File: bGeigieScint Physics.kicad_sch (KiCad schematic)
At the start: 15 parts, among them P1 Header-Male-2.54_2x2, P2 Header-Male-2.54_2x2, U1 TMP116xxDRV, U2 AT24CS01-STUM, U3 BroadCOM SiPM 4x4

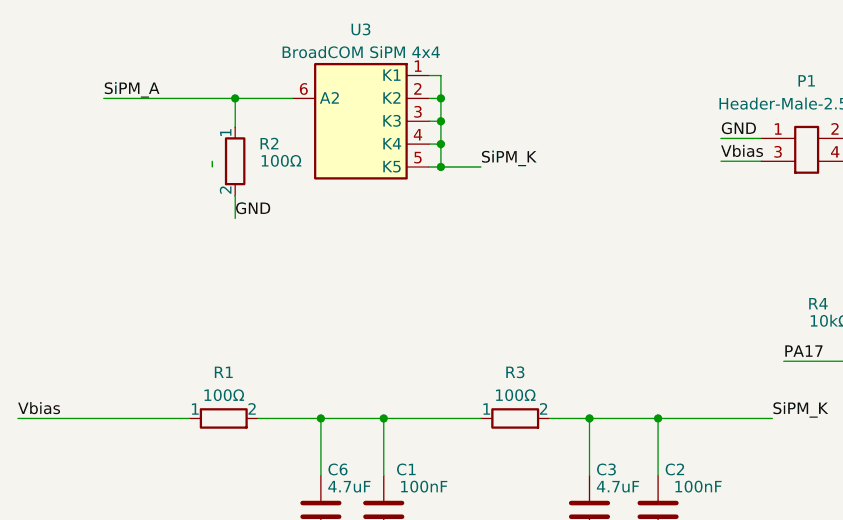
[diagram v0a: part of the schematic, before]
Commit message: Add AFBRS4N44P014M component to KiCad libraries
- Created new module file for AFBRS4N44P014M in Kicad libs with detailed footprint and pad definitions.
- Added corresponding module entry in the bGeigieScint.pretty library.
- Updated fp-lib-table to include new library paths for proper integration.
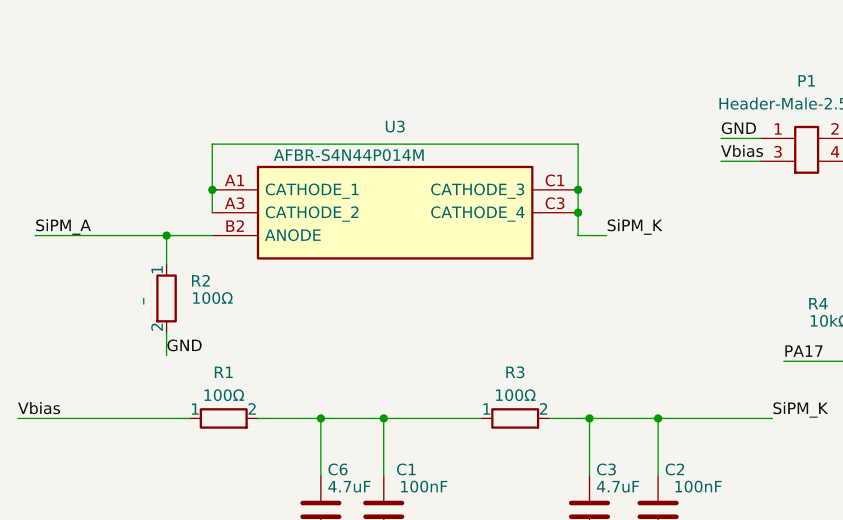
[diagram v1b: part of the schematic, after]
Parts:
- removed U3: BroadCOM SiPM 4x4, symbol SiPM_4x4
- added U3: AFBR-S4N44P014M, AFBRS4N44P014M, symbol AFBR-S4N44P014M:AFBR-S4N44P014M
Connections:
- net SiPM_A: now also U3.B2 (ANODE)
- net SiPM_K: now also U3.A1 (CATHODE_1), U3.A3 (CATHODE_2), U3.C1 (CATHODE_3), U3.C3 (CATHODE_4)
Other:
- moved on the sheet: R2

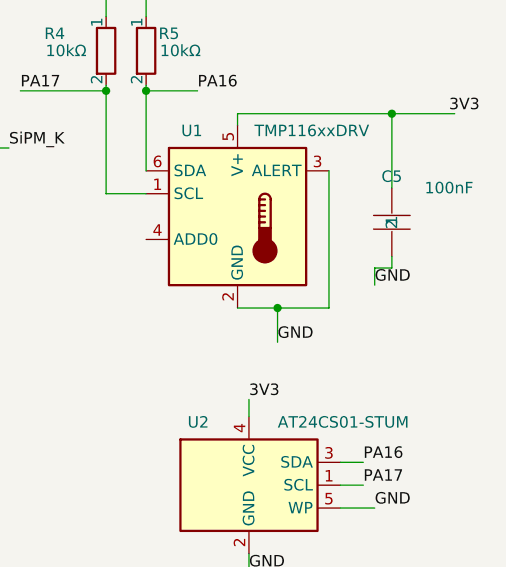
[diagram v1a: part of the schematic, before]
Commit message: refactor: Remove unused schematic symbol definitions, add a 3D model, and update KiCad schematic and PCB files.
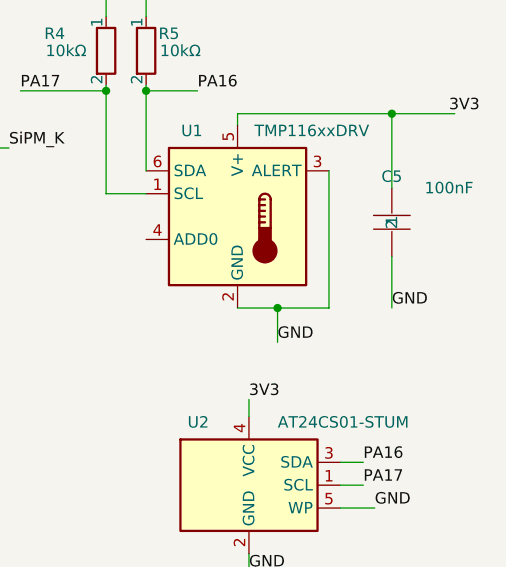
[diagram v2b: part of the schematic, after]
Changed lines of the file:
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@@
-	(wire
-		(pts
-			(xy 167.005 113.665) (xy 167.005 114.935)
-		)
-		(stroke
-			(width 0)
-			(type default)
-		)
-	)
 	(wire
 		(pts
@@
 	(wire
 		(pts
-			(xy 167.005 114.935) (xy 165.1 114.935)
-		)
-		(stroke
-			(width 0)
-			(type default)
-		)
-	)
-	(wire
-		(pts
 			(xy 74.295 101.6) (xy 74.295 107.95)
 		)
@@
 	(wire
 		(pts
-			(xy 165.1 114.935) (xy 165.1 116.84)
+			(xy 167.005 113.665) (xy 167.005 119.38)
 		)
 		(stroke
@@
 	)
 	(label "GND"
-		(at 165.1 116.84 0)
-		(effects
-			(font
+		(at 167.005 119.38 0)
+		(effects
+			(font

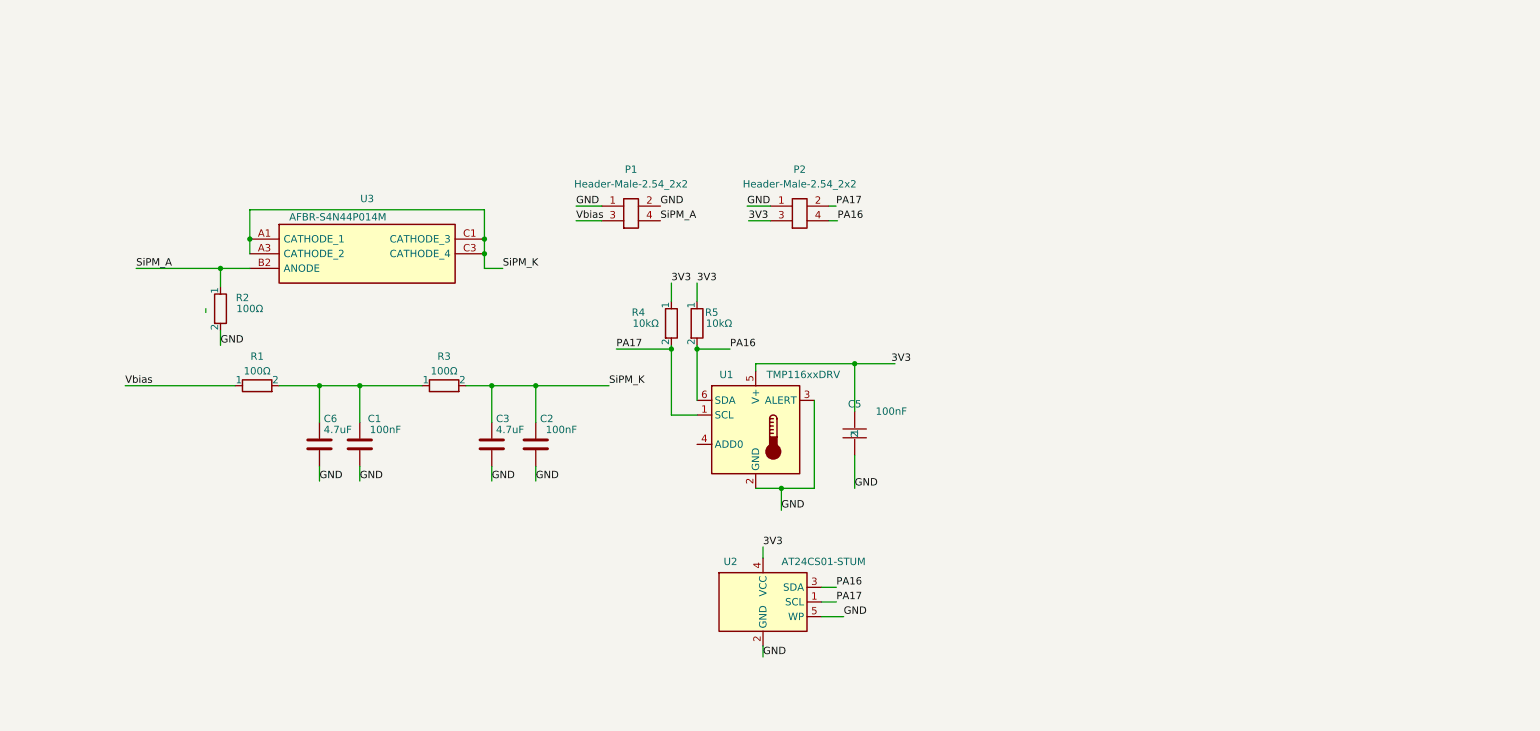
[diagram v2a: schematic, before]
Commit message: feat: Add new KiCad component libraries and update schematic/PCB.
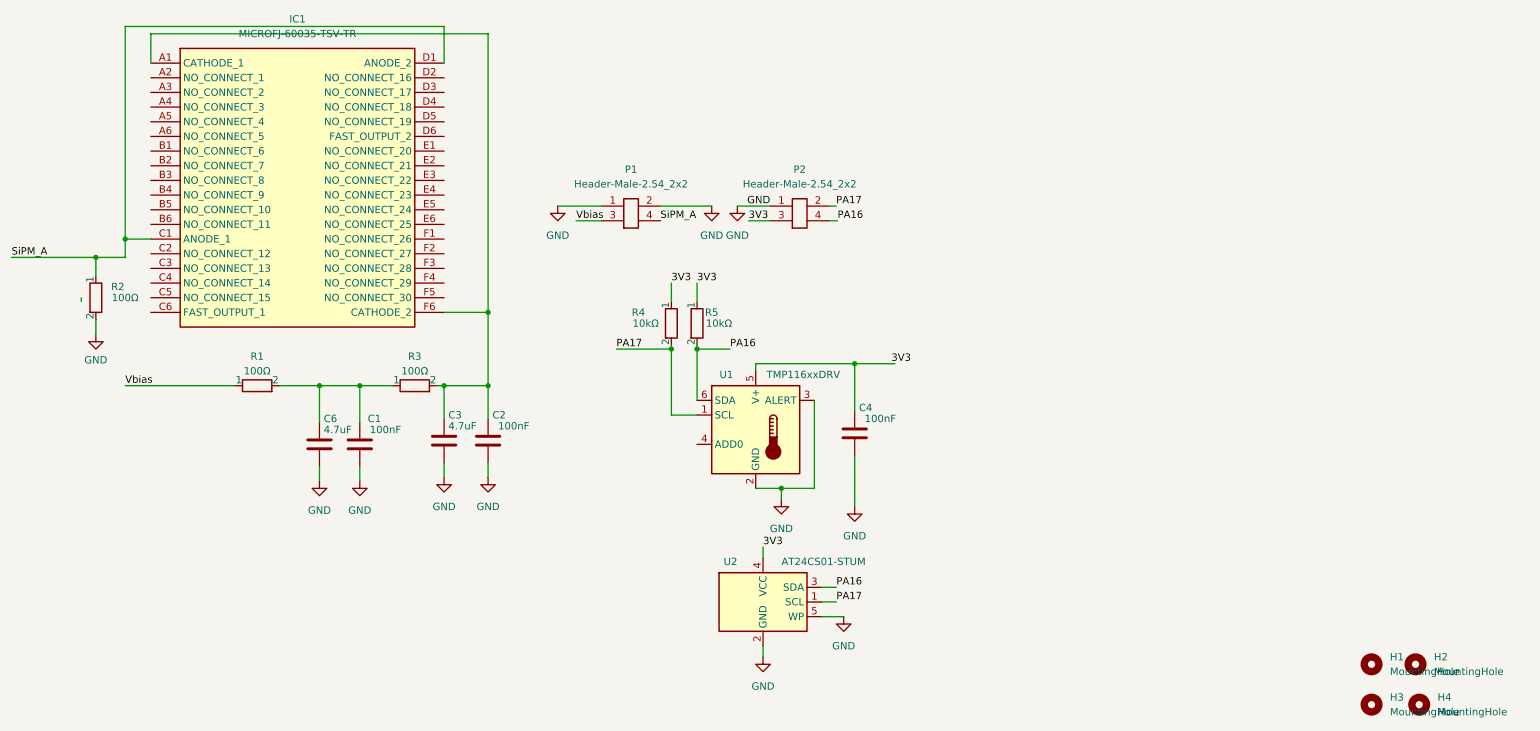
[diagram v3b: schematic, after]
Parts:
- removed C5: 100nF, symbol C_0603
- removed U3: AFBR-S4N44P014M, AFBRS4N44P014M, symbol AFBR-S4N44P014M:AFBR-S4N44P014M
- added C4: 100nF, Capacitor_SMD:C_0805_2012Metric, symbol Device:C
- added H1, H2, H3, H4: MountingHole, MountingHole:MountingHole_3.2mm_M3, symbol Mechanical:MountingHole
- added IC1: MICROFJ-60035-TSV-TR, bGeigieScint:BGA36C100P6X6_613X613X67, symbol MICROFJ-60035-TSV-TR:MICROFJ-60035-TSV-TR
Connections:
- net 3V3: now also C4.1
- net GND: now also C4.2
- net SiPM_A: now also IC1.C1 (ANODE_1), IC1.D1 (ANODE_2)
- net SiPM_K: no longer names the net of C2.1, C3.1, R3.2
- net SiPM_K: now also IC1.A1 (CATHODE_1), IC1.F6 (CATHODE_2)
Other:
- moved on the sheet: C2, C3, R2, R3

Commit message: feat: Assign footprints to schematic components, add a new net, and place pin headers on the PCB while adjusting a mounting hole.
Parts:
- P1, P2: footprint (none) -> Connector_PinHeader_2.54mm:PinHeader_2x02_P2.54mm_Vertical
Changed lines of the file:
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@@
 			)
 		)
-		(property "Footprint" ""
+		(property "Footprint" "Connector_PinHeader_2.54mm:PinHeader_2x02_P2.54mm_Vertical"
 			(at 157.48 71.755 0)
 			(effects
@@
 					(size 1.27 1.27)
 				)
+				(hide yes)
 			)
 		)
@@
 			)
 		)
-		(property "Footprint" ""
+		(property "Footprint" "Connector_PinHeader_2.54mm:PinHeader_2x02_P2.54mm_Vertical"
 			(at 128.27 71.755 0)
 			(effects
@@
 					(size 1.27 1.27)
 				)
-			)
-		)
+				(hide yes)
+			)
+		)
